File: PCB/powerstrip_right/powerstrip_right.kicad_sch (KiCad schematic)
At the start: 0 parts

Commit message: random upload
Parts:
- added C1: C, Capacitor_SMD:C_1206_3216Metric_Pad1.33x1.80mm_HandSolder, symbol Device:C
- added C10, C11, C3, C4, C5, C6, C7, C8, C9: C_Polarized, Capacitor_THT:CP_Radial_D5.0mm_P2.50mm, symbol Device:C_Polarized
- added IC1: PCA9685PW_Q900,118, Power_Strip_Library:SOP65P640X110-28N, symbol Power_Strip_Library:PCA9685PW_Q900,118
- added J1: XT60PW-M, Power_Strip_Library:AMASS_XT60PW-M, symbol Power_Strip_Library:XT60PW-M
- added J2, J3, J4: Conn_01x06_Pin, Connector_PinHeader_2.54mm:PinHeader_1x06_P2.54mm_Vertical, symbol Connector:Conn_01x06_Pin
- added J5, J6, J7: Conn_01x03_Pin, Connector_PinHeader_2.54mm:PinHeader_1x03_P2.54mm_Vertical, symbol Connector:Conn_01x03_Pin
- added J8: Conn_01x08_Pin, Connector_FFC-FPC:Amphenol_F32Q-1A7x1-11008_1x08-1MP_P0.5mm_Horizontal, symbol Connector:Conn_01x08_Pin
- added J9: Conn_01x02_Pin, Connector_JST:JST_XH_B2B-XH-AM_1x02_P2.50mm_Vertical, symbol Connector:Conn_01x02_Pin
- added R1, R2, R3, R4, R6, R7, R8, R9: GMR50HJAAFD5L00, Power_Strip_Library:GMR50HJAAFD5L00, symbol Power_Strip_Library:GMR50HJAAFD5L00
- added U1: MUX508IDR, Power_Strip_Library:SOIC127P600X175-16N, symbol Power_Strip_Library:MUX508IDR
- added U2: INA181, Package_TO_SOT_SMD:SOT-23-6, symbol Amplifier_Current:INA181
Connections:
- new net: C1.1, U1.8 (D), U2.3 (+)
- new net 3.3V: IC1.1 (A0), IC1.28 (VDD), IC1.3 (A2), IC1.5 (A4), U1.13 (VDD), U2.6 (V+)
- new net A0: J8.4 (Pin_4), U1.1 (A0)
- new net A1: J8.3 (Pin_3), U1.16 (A1)
- new net A2: J8.2 (Pin_2), U1.15 (A2)
- new net ADC INPUT: J8.8 (Pin_8), U2.1
- new net GND: C1.2, C10.2, C11.2, C3.2, C4.2, C5.2, C6.2, C7.2, C8.2, C9.2, IC1.14 (VSS), IC1.2 (A1), IC1.24 (A5), IC1.4 (A3), J1.2 (-), J2.2 (Pin_2), J8.1 (Pin_1), J9.1 (Pin_1), R1.2, R2.2, R3.2, R4.2, R6.2, R7.2, R8.2, R9.2, U1.14 (GND), U1.2 (EN), U1.3 (VSS), U2.2 (GND), U2.4 (-), U2.5 (REF)
- new net GND_SERVO1: J5.1 (Pin_1), R1.1, U1.4 (S1)
- new net GND_SERVO2: J5.2 (Pin_2), R2.1, U1.5 (S2)
- new net GND_SERVO3: J5.3 (Pin_3), R3.1, U1.6 (S3)
- new net GND_SERVO4: J2.1 (Pin_1), R4.1, U1.7 (S4)
- new net GND_SERVO6: J2.3 (Pin_3), R6.1, U1.12 (S5)
- new net GND_SERVO7: J2.4 (Pin_4), R7.1, U1.11 (S6)
- new net GND_SERVO8: J2.5 (Pin_5), R8.1, U1.10 (S7)
- new net GND_SERVO9: J2.6 (Pin_6), R9.1, U1.9 (S8)
- new net PWM_SERVO1: IC1.6 (LED0), J7.1 (Pin_1)
- new net PWM_SERVO2: IC1.7 (LED1), J7.2 (Pin_2)
- new net PWM_SERVO3: IC1.8 (LED2), J7.3 (Pin_3)
- new net PWM_SERVO4: IC1.9 (LED3), J4.1 (Pin_1)
- new net PWM_SERVO5: IC1.10 (LED4), J4.2 (Pin_2)
- new net PWM_SERVO6: IC1.11 (LED5), J4.3 (Pin_3)
- new net PWM_SERVO7: IC1.12 (LED6), J4.4 (Pin_4)
- new net PWM_SERVO8: IC1.13 (LED7), J4.5 (Pin_5)
- new net PWM_SERVO9: IC1.15 (LED8), J4.6 (Pin_6)
- new net SCL: IC1.26 (SCL), J8.6 (Pin_6)
- new net SDA: IC1.27 (SDA), J8.5 (Pin_5)
- new net VCC: C10.1, C11.1, C3.1, C4.1, C5.1, C6.1, C7.1, C8.1, C9.1, J1.1 (+), J3.1 (Pin_1), J3.2 (Pin_2), J3.3 (Pin_3), J3.4 (Pin_4), J3.5 (Pin_5), J3.6 (Pin_6), J6.1 (Pin_1), J6.2 (Pin_2), J6.3 (Pin_3), J9.2 (Pin_2)
- new net ¬EN: IC1.23 (~{OE}), J8.7 (Pin_7)
- no-connect marks 0 -> 8

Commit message: Stripe PCB's
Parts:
- removed R1, R2, R3, R4, R6, R7, R8, R9: GMR50HJAAFD5L00, Power_Strip_Library:GMR50HJAAFD5L00, symbol Power_Strip_Library:GMR50HJAAFD5L00
- added C12, C13, C2: 100n, Capacitor_SMD:C_0201_0603Metric_Pad0.64x0.40mm_HandSolder, symbol Device:C
- added C14: 1u, Capacitor_SMD:C_1206_3216Metric_Pad1.33x1.80mm_HandSolder, symbol Device:C
- added C15: 10u Tantal, Capacitor_SMD:C_1206_3216Metric_Pad1.33x1.80mm_HandSolder, symbol Device:C
- added U3: LT1117CST-3.3, PCM_Package_TO_SOT_SMD_AKL:SOT-223-3_TabPin2, symbol PCM_Voltage_Regulator_AKL:LT1117CST-3.3
- added shunt_01, shunt_2, shunt_3, shunt_4, shunt_5, shunt_6, shunt_7, shunt_8: R0.005, Resistor_SMD:R_0201_0603Metric_Pad0.64x0.40mm_HandSolder, symbol Device:R
- C1: value C -> 100n; footprint Capacitor_SMD:C_1206_3216Metric_Pad1.33x1.80mm_HandSolder -> Capacitor_SMD:C_0201_0603Metric_Pad0.64x0.40mm_HandSolder
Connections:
- net 3.3V: now also C12.2, C13.1, C15.1, C2.1, U3.2 (OUT)
- net GND: now also C12.1, C13.2, C14.2, C15.2, C2.2, U3.1, shunt_01.2, shunt_2.2, shunt_3.2, shunt_4.2, shunt_5.2, shunt_6.2, shunt_7.2, shunt_8.2
- net GND_SERVO1: now also shunt_01.1
- net GND_SERVO2: now also shunt_2.1
- net GND_SERVO3: now also shunt_3.1
- net GND_SERVO4: now also shunt_4.1
- net GND_SERVO6: now also shunt_5.1
- net GND_SERVO7: now also shunt_6.1
- net GND_SERVO8: now also shunt_7.1
- net GND_SERVO9: now also shunt_8.1
- net VCC: now also C14.1, U3.3 (IN)
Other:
- moved on the sheet: J8, J9

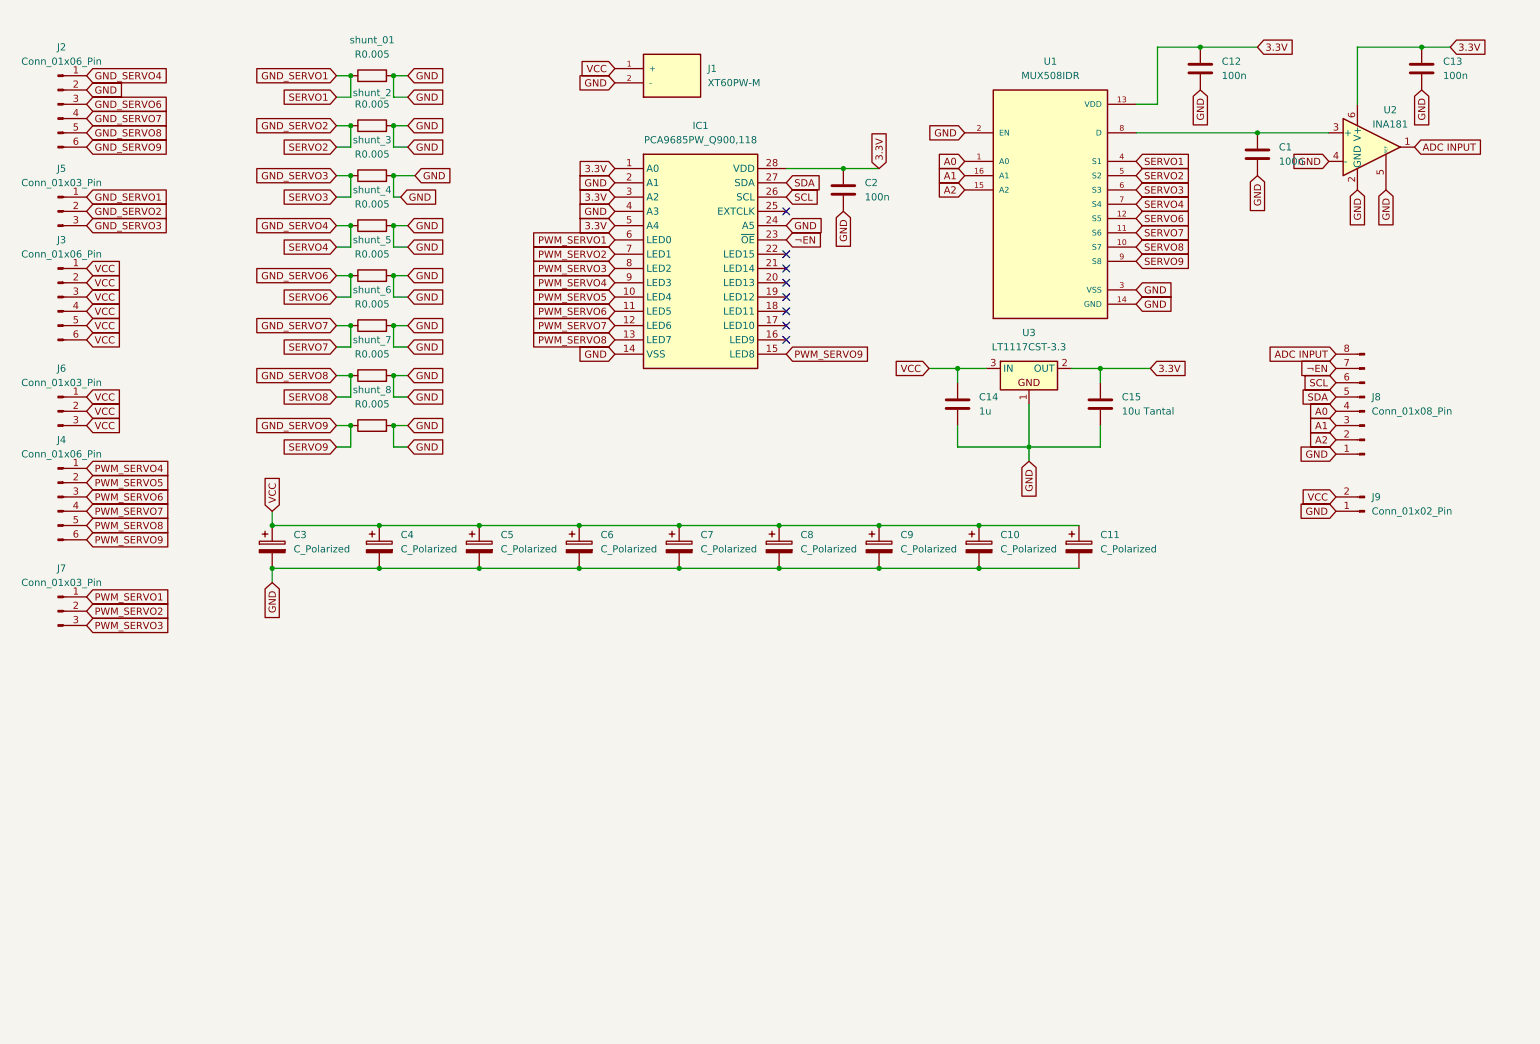
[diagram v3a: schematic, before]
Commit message: Stop tracking renders folder & final Powerstrip and Mainboard PCB
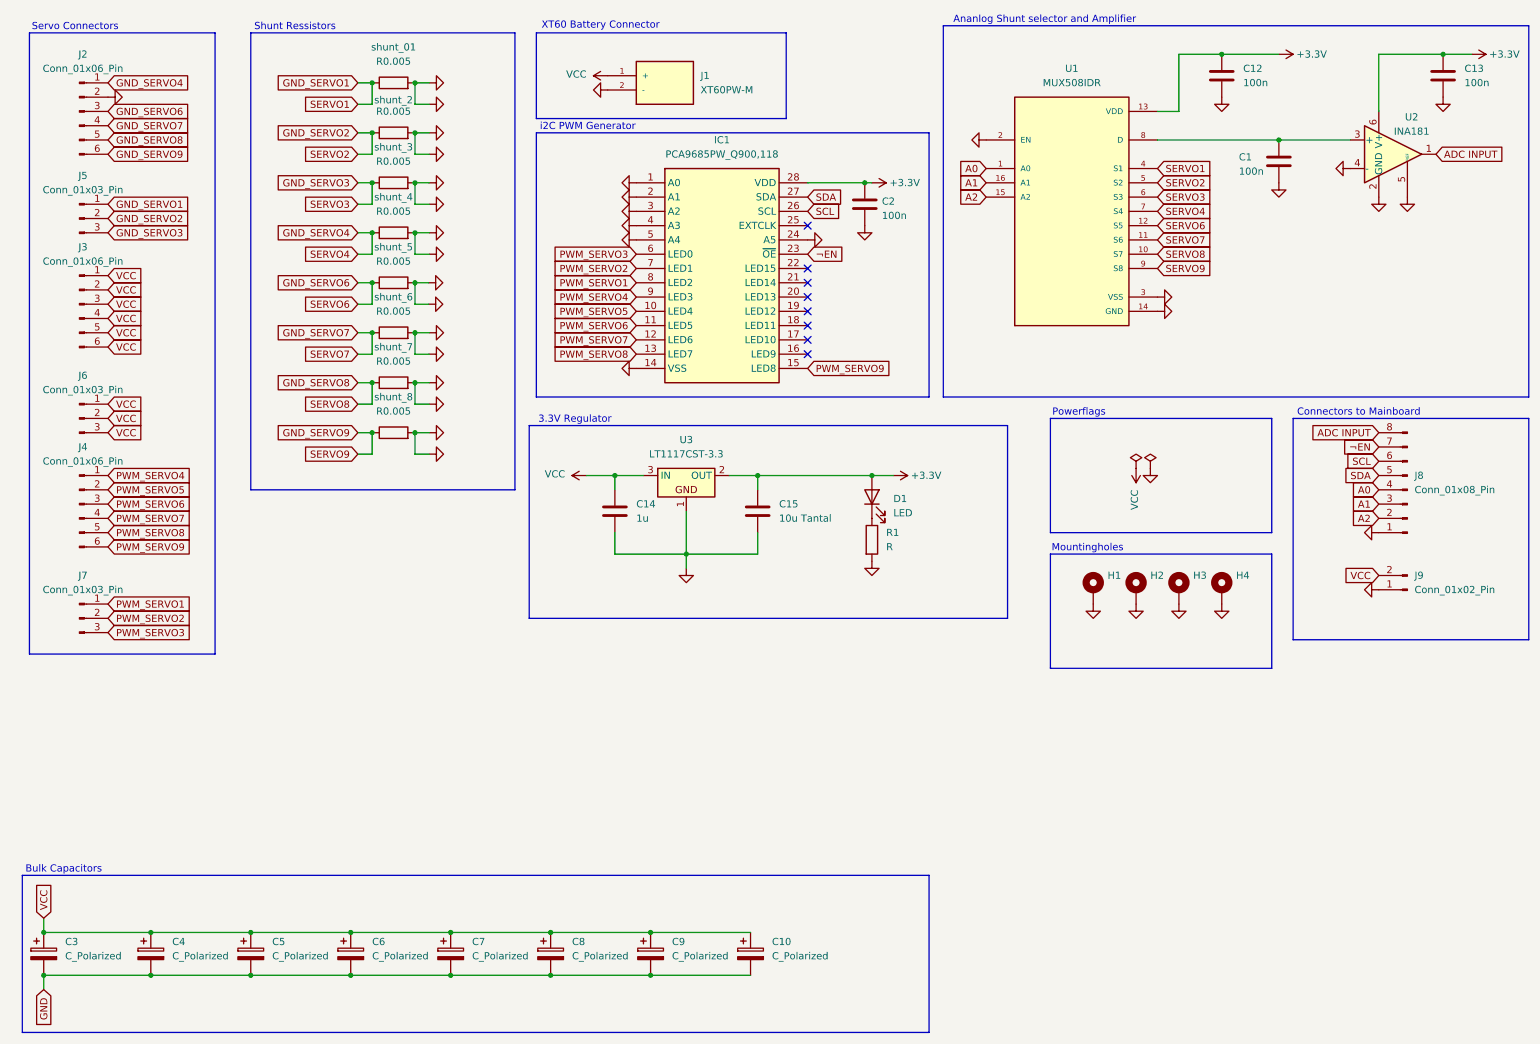
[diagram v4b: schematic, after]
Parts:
- removed C11: C_Polarized, Capacitor_THT:CP_Radial_D5.0mm_P2.50mm, symbol Device:C_Polarized
- added D1: LED, Power_Strip_Library:LEDC1608X70N, symbol Device:LED
- added H1, H2, H3, H4: MountingHole_Pad, MountingHole:MountingHole_3.5mm_Pad_Via, symbol Mechanical:MountingHole_Pad
- added R1: R, Resistor_SMD:R_0402_1005Metric_Pad0.72x0.64mm_HandSolder, symbol Device:R
- C1, C12, C13, C2: footprint Capacitor_SMD:C_0201_0603Metric_Pad0.64x0.40mm_HandSolder -> Capacitor_SMD:C_0402_1005Metric_Pad0.74x0.62mm_HandSolder
- J8: footprint Connector_FFC-FPC:Amphenol_F32Q-1A7x1-11008_1x08-1MP_P0.5mm_Horizontal -> Power_Strip_Library:17352658
- U3: footprint PCM_Package_TO_SOT_SMD_AKL:SOT-223-3_TabPin2 -> Power_Strip_Library:SOT230P700X180-4N
- shunt_01, shunt_2, shunt_3, shunt_4, shunt_5, shunt_6, shunt_7, shunt_8: footprint Resistor_SMD:R_0201_0603Metric_Pad0.64x0.40mm_HandSolder -> Resistor_SMD:R_1206_3216Metric_Pad1.30x1.75mm_HandSolder
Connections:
- net GND: now also IC1.1 (A0), IC1.3 (A2), IC1.5 (A4), H1.1, H2.1, H3.1, H4.1, R1.2
- net PWM_SERVO1: now also IC1.8 (LED2); no longer IC1.6 (LED0)
- net PWM_SERVO3: now also IC1.6 (LED0); no longer IC1.8 (LED2)
- net 3.3V renamed +3.3V
- net +3.3V: now also D1.2 (A); no longer IC1.1 (A0), IC1.3 (A2), IC1.5 (A4)
- new net: D1.1 (K), R1.1
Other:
- note added: "3.3V Regulator"
- note added: "Ananlog Shunt selector and Amplifier"
- note added: "Bulk Capacitors"
- note added: "Connectors to Mainboard"
- note added: "Mountingholes"
- note added: "Powerflags"
- note added: "Servo Connectors"
- note added: "Shunt Ressistors"
- note added: "XT60 Battery Connector"
- note added: "i2C PWM Generator"
- moved on the sheet: C1, C10, C12, C13, C14, C15, C2, C3, C4, C5, C6, C7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
